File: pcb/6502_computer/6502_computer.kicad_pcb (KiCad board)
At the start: 2 copper layers, 116.8 x 73.7 mm, 44 parts, among them J1 Conn_02x04_Odd_Even, J2 USB_B, J3 Conn_02x20_Odd_Even, J4 Conn_01x04, J5 Conn_01x02, SW1 SW_Push, SW2 SW_Push, SW3 SW_Push, U1 6502, U10 CH340N, U11 MC6840, U2 6551, U3 74LS139, U4 74LS138, U5 CY62256-70PC, U6 27C64, U7 74LS00, U8 DS1813-5+, U9 74LS93, X1 ACO-xxxMHz, Y1 1.8432MHz

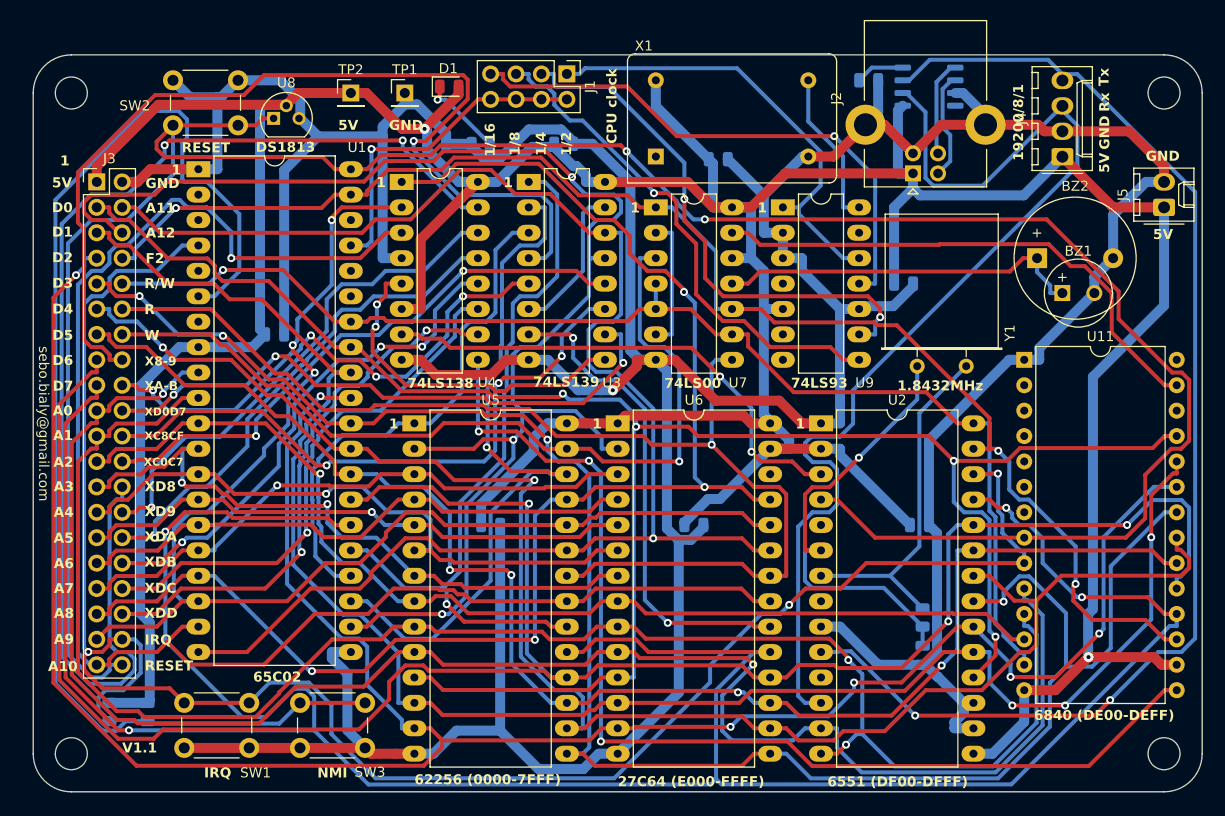
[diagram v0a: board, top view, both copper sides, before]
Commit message: silkscreen fixes
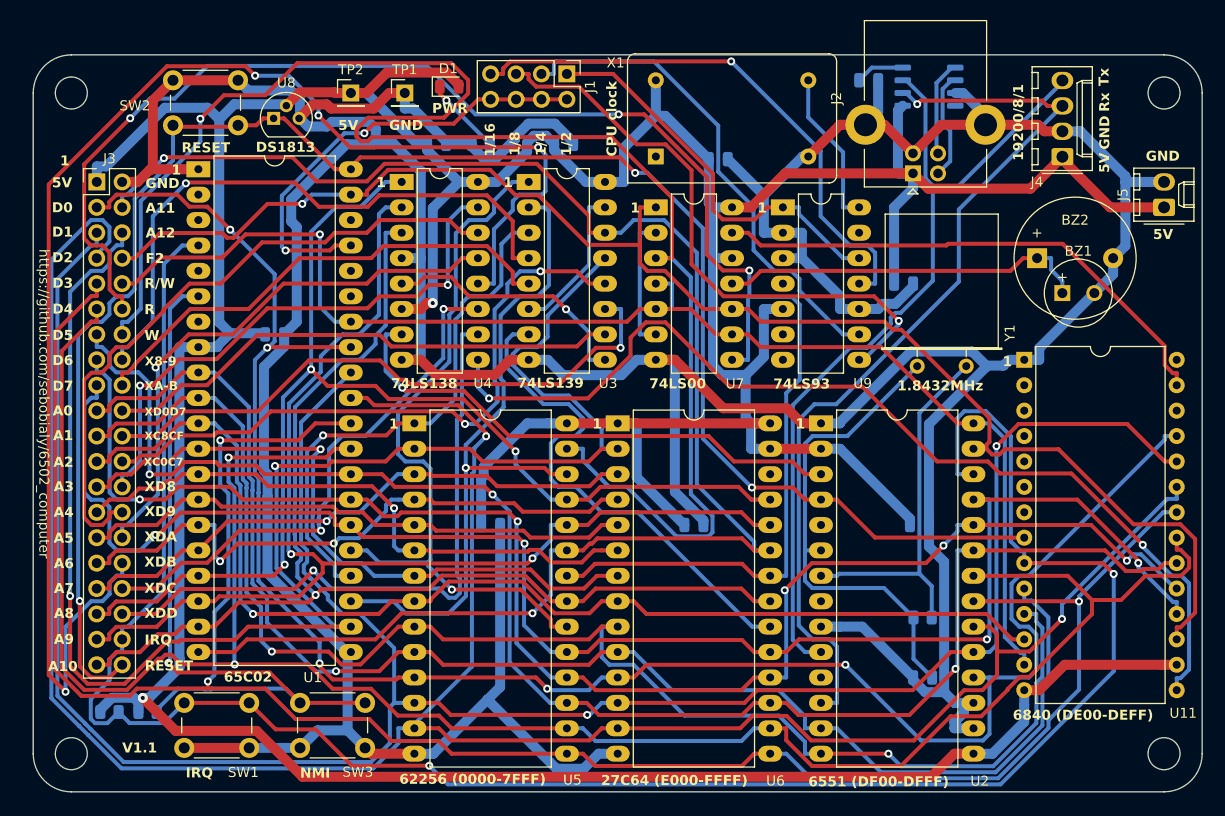
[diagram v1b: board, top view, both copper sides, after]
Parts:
- moved C1 2.22 mm to (153.7, 99.1), turned to 0 degrees
- turned R1 to 180 degrees
- turned R2 to 180 degrees
- turned R4 to 180 degrees
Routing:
- net /D7: track 272.1 -> 162.2 mm
- net /XDB: track 51.2 -> 144.4 mm, vias 3 -> 4
- net /W: track 86.5 -> 161.4 mm
- net /RES: track 247.4 -> 181.0 mm, vias 2 -> 3
- net /XD8: track 122.1 -> 56.1 mm
- net /D6: track 215.7 -> 153.3 mm, vias 3 -> 5
- net /D1: track 176.2 -> 233.5 mm, vias 3 -> 2
- net VCC: track 435.5 -> 488.0 mm
- net /D4: track 166.4 -> 218.2 mm
- net /R: track 115.8 -> 167.1 mm, vias 1 -> 3
- net /NMI: track 124.0 -> 76.2 mm, vias 0 -> 1
- net /A10: track 158.7 -> 117.2 mm
- net /TxD: track 124.1 -> 85.2 mm, vias 2 -> 0
- net /D3: track 187.9 -> 226.1 mm, vias 4 -> 3
- net /X89: track 98.3 -> 61.1 mm
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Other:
- board text added: "PWR"
- board text added: "https://github.com/sebobialy/6502_computer"
- board text removed: "sebo.bialy@gmail.com"

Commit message: added timer outputs from 6840
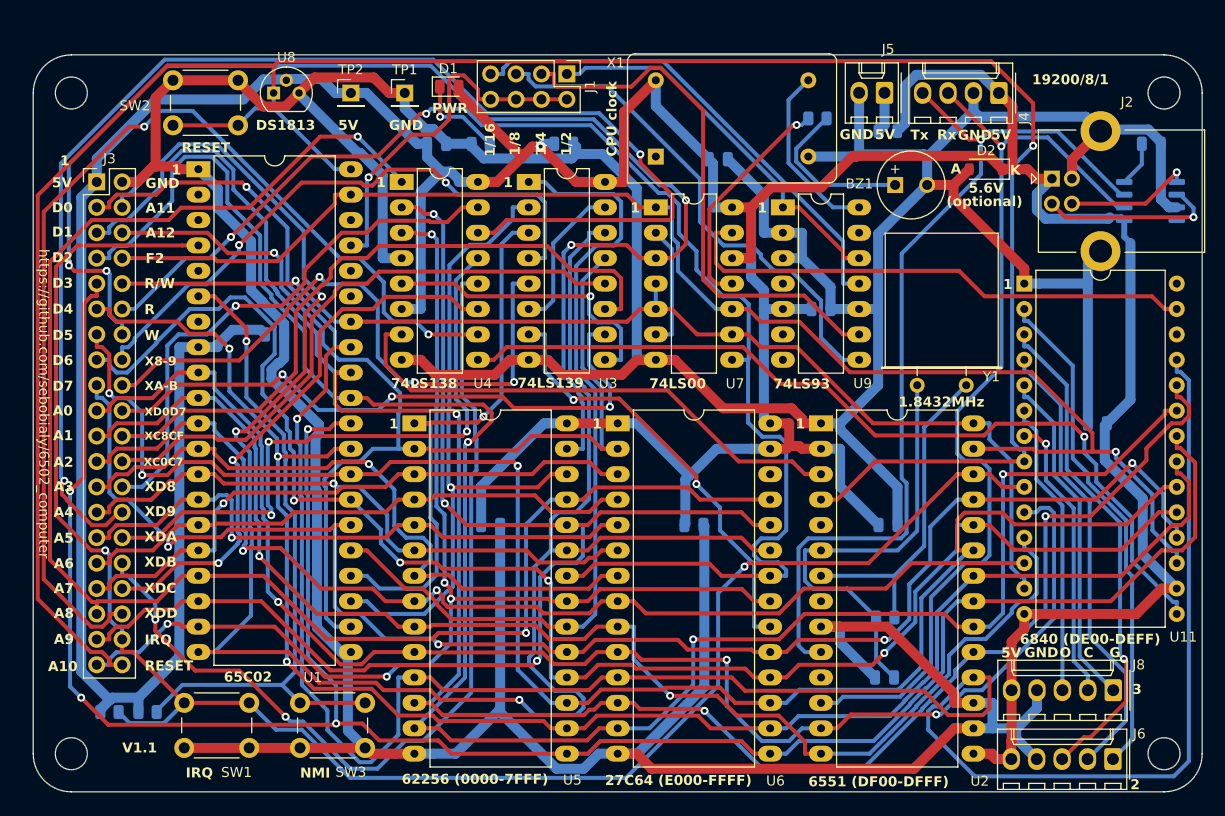
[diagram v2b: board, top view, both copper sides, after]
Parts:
- removed BZ2: Buzzer, Buzzer_Beeper:Buzzer_12x9.5RM7.6
- added C11: 100n, Capacitor_SMD:C_0805_2012Metric, B.Cu at (171.1, 73.7)
- added D2: 5.6V, Diode_SMD:D_SOD-123, F.Cu at (160.0, 48.3)
- added F1: Polyfuse, Fuse:Fuse_0805_2012Metric, B.Cu at (150.2, 44.5)
- added J6: Conn_01x05, Connector_Molex:Molex_KK-254_AE-6410-05A_1x05_P2.54mm_Vertical, F.Cu at (172.7, 107.2)
- added J8: Conn_01x05, Connector_Molex:Molex_KK-254_AE-6410-05A_1x05_P2.54mm_Vertical, F.Cu at (172.7, 100.3)
- added R5: 1k, Resistor_SMD:R_0805_2012Metric, B.Cu at (143.2, 43.2)
- moved J5 30.2 mm to (149.9, 40.6), turned to 180 degrees
- moved C2 29.0 mm to (176.5, 45.7)
- moved U10 24.9 mm to (176.4, 51.4)
- moved BZ1 19.9 mm to (150.9, 49.8)
- moved J2 13.9 mm to (166.6, 49.2), turned to 0 degrees
- moved J4 8.99 mm to (161.3, 40.6), turned to 180 degrees
- moved C10 8.64 mm to (143.5, 62.2)
- moved U11 7.62 mm to (163.8, 59.7)
- moved C1 3.81 mm to (149.9, 99.1)
- moved R4 3.74 mm to (149.9, 93.1)
- moved C5 3.14 mm to (150.2, 83.8)
- moved U8 2.54 mm to (88.8, 40.6)
- moved Y1 1.91 mm to (158.0, 69.8)
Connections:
- J5 pad 1: VCC -> /5V
- U11 pad 2: unconnected-(U11-~{G2}-Pad2) -> Net-(J6-Pin_1)
- U11 pad 3: unconnected-(U11-O2-Pad3) -> Net-(J6-Pin_3)
- U11 pad 4: unconnected-(U11-~{C2}-Pad4) -> Net-(J6-Pin_2)
- U11 pad 5: unconnected-(U11-~{G3}-Pad5) -> Net-(J8-Pin_1)
- U11 pad 6: unconnected-(U11-O3-Pad6) -> Net-(J8-Pin_3)
- U11 pad 7: unconnected-(U11-~{C3}-Pad7) -> Net-(J8-Pin_2)
- U7 pad 11: Net-(BZ1-+) -> Net-(R5-Pad1)
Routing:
- net GND: track 507.5 -> 581.2 mm
- net /XD9: track 66.0 -> 135.1 mm, vias 0 -> 2
- net /RES: track 181.0 -> 243.2 mm, vias 3 -> 1
- net /XDB: track 144.4 -> 92.2 mm, vias 4 -> 2
- net /A12: track 164.5 -> 113.5 mm, vias 2 -> 1
- net Net-(J6-Pin_1): track 0.00 -> 50.5 mm
- net Net-(J6-Pin_3): track 0.00 -> 49.9 mm, vias 0 -> 1
- net /D4: track 218.2 -> 168.9 mm, vias 2 -> 3
- net /D0: track 190.9 -> 239.6 mm, vias 5 -> 2
- net Net-(J6-Pin_2): track 0.00 -> 45.9 mm
- net /A8: track 119.9 -> 163.8 mm, vias 3 -> 2
- net /XDD: track 64.7 -> 105.9 mm, vias 1 -> 2
- net /D2: track 241.1 -> 200.7 mm, vias 2 -> 3
- net Net-(J8-Pin_1): track 0.00 -> 34.4 mm
- net /D1: track 233.5 -> 200.1 mm, vias 2 -> 3
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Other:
- board text added: "(optional)"
- board text added: "2"
- board text added: "3"
- board text added: "5.6V"
- board text added: "A"
- board text added: "C"
- board text added: "G"
- board text added: "K"
- board text added: "O"

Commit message: fixed problem with not negating E for 74LS139. Buzzer is now using a transistor. 6502 is ZIF friendly.
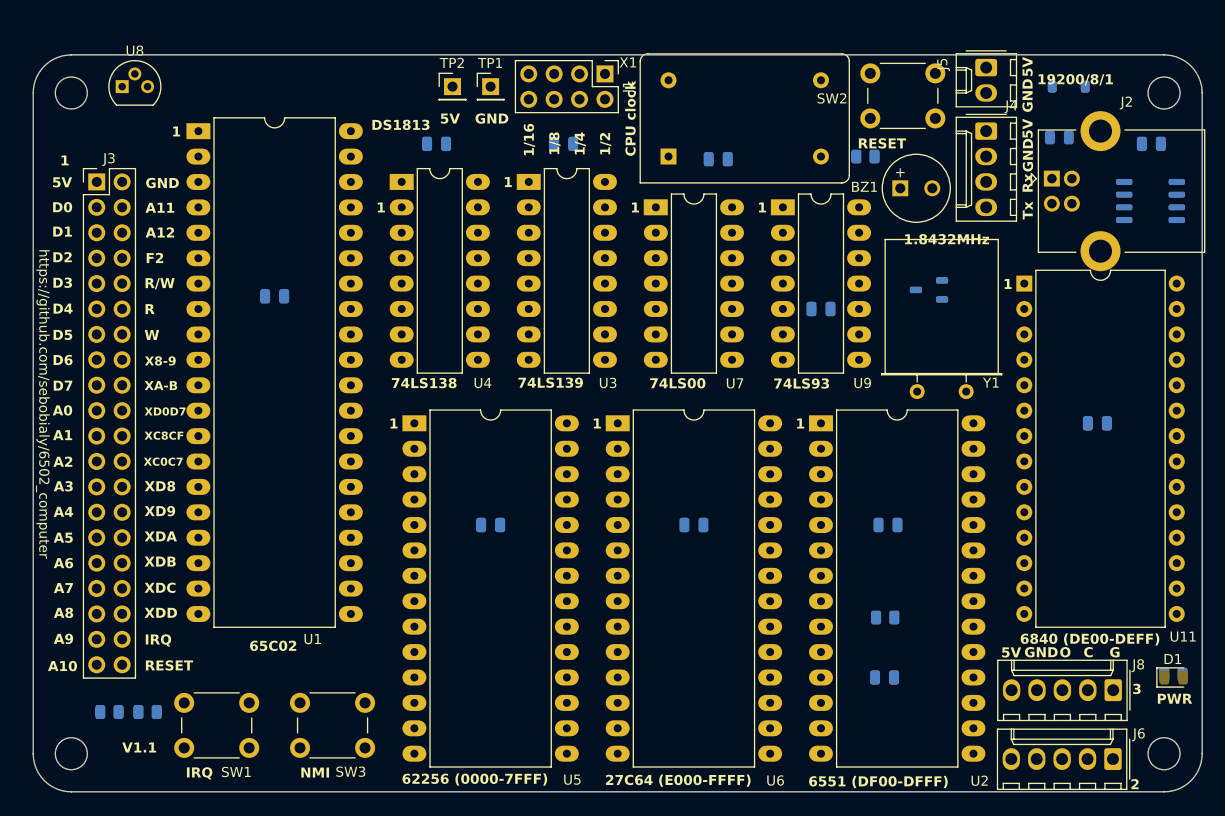
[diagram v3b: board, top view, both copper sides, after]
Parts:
- added Q1: NPN, Package_TO_SOT_SMD:TSOT-23, B.Cu at (154.3, 60.3)
- D2: moved to B.Cu
- moved D1 93.4 mm to (178.8, 99.1)
- moved R3 87.2 mm to (178.7, 98.8)
- moved SW2 69.7 mm to (148.4, 38.7)
- moved F1 17.2 mm to (167.3, 45.1)
- moved U8 15.2 mm to (73.7, 40.0)
- moved D2 11.7 mm to (168.3, 40.0), turned to 0 degrees
- moved J5 10.5 mm to (160.0, 38.1), turned to -90 degrees
- moved TP2 10.2 mm to (106.7, 40.0)
- moved TP1 8.61 mm to (110.5, 40.0)
- moved R5 6.13 mm to (148.0, 47.0)
- moved J4 4.02 mm to (160.0, 44.5), turned to -90 degrees
- moved J1 3.81 mm to (121.9, 38.7)
- moved U1 3.80 mm to (81.3, 44.5)
- moved C7 3.80 mm to (88.9, 61.0)
- moved X1 1.27 mm to (128.3, 47.0)
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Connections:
- BZ1 pad 1: Net-(BZ1-+) -> VCC
- BZ1 pad 2: GND -> Net-(BZ1--)
- R5 pad 1: Net-(R5-Pad1) -> /BUZZ
- R5 pad 2: Net-(BZ1-+) -> Net-(Q1-B)
- U3 pad 1: /A15 -> Net-(U3A-E)
- U7 pad 11: Net-(R5-Pad1) -> Net-(U3A-E)
- U7 pad 12: VCC -> /A15
- U7 pad 13: /BUZZ -> /A15
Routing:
- net GND: track 581.2 -> 0.00 mm
- net VCC: track 472.1 -> 0.00 mm, vias 1 -> 0
- net /RES: track 243.2 -> 0.00 mm, vias 1 -> 0
- net /D0: track 239.6 -> 0.00 mm, vias 2 -> 0
- net /D3: track 216.7 -> 0.00 mm, vias 4 -> 0
- net /D2: track 200.7 -> 0.00 mm, vias 3 -> 0
- net /D1: track 200.1 -> 0.00 mm, vias 3 -> 0
- net /A11: track 197.8 -> 0.00 mm, vias 3 -> 0
- net /IRQ: track 179.2 -> 0.00 mm, vias 2 -> 0
- net /D4: track 168.9 -> 0.00 mm, vias 3 -> 0
- net /D5: track 164.1 -> 0.00 mm, vias 3 -> 0
- net /A8: track 163.8 -> 0.00 mm, vias 2 -> 0
- net /D6: track 157.3 -> 0.00 mm, vias 4 -> 0
- net /D7: track 153.1 -> 0.00 mm, vias 4 -> 0
- net /A0: track 146.2 -> 0.00 mm, vias 3 -> 0
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
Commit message: routed 1.2 version
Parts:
- moved U8 34.8 mm to (108.0, 45.7)
- moved C6 2.86 mm to (102.2, 45.7)
- moved J3 1.27 mm to (69.8, 49.5)
- moved H2 1.27 mm to (67.3, 106.7)
- moved H4 1.27 mm to (67.3, 40.6)
- moved SW1 0.93 mm to (86.4, 107.0)
- moved SW3 0.93 mm to (97.9, 107.0)
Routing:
- net GND: track 0.00 -> 562.6 mm, vias 0 -> 1
- net VCC: track 0.00 -> 484.4 mm, vias 0 -> 4
- net /D1: track 0.00 -> 268.0 mm, vias 0 -> 3
- net /D2: track 0.00 -> 229.0 mm, vias 0 -> 3
- net /D3: track 0.00 -> 215.6 mm
- net /D4: track 0.00 -> 207.3 mm, vias 0 -> 3
- net /D0: track 0.00 -> 204.8 mm, vias 0 -> 2
- net /D6: track 0.00 -> 202.6 mm, vias 0 -> 3
- net /D7: track 0.00 -> 195.3 mm, vias 0 -> 4
- net /RES: track 0.00 -> 192.4 mm, vias 0 -> 1
- net /D5: track 0.00 -> 180.6 mm, vias 0 -> 4
- net /IRQ: track 0.00 -> 176.6 mm, vias 0 -> 2
- net /R: track 0.00 -> 163.5 mm, vias 0 -> 3
- net /W: track 0.00 -> 150.6 mm, vias 0 -> 4
- net /A11: track 0.00 -> 148.3 mm
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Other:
- board size 116.8 x 73.7 mm -> 118.1 x 73.7 mm
- board text added: "V1.2"
- board text removed: "V1.1"

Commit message: routed v1.2
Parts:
- moved U4 1.27 mm to (102.9, 49.5)
- moved C10 0.65 mm to (142.9, 62.2)
- moved U9 0.65 mm to (139.1, 52.1)
- moved U3 0.62 mm to (114.9, 49.5)
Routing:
- net /XD0D7: track 130.5 -> 54.2 mm, vias 3 -> 1
- net /W: track 150.6 -> 86.4 mm, vias 4 -> 3
- net /D6: track 202.6 -> 145.2 mm, vias 3 -> 2
- net /D7: track 195.3 -> 141.1 mm, vias 4 -> 2
- net /R: track 163.5 -> 110.6 mm, vias 3 -> 0
- net /XC8CF: track 61.1 -> 111.1 mm
- net /D3: track 215.6 -> 170.3 mm, vias 0 -> 2
- net /D4: track 207.3 -> 165.2 mm, vias 3 -> 2
- net GND: track 562.6 -> 527.4 mm, vias 1 -> 2
- net /A11: track 148.3 -> 183.4 mm, vias 0 -> 1
- net VCC: track 484.4 -> 452.6 mm, vias 4 -> 2
- net /D1: track 268.0 -> 237.9 mm, vias 3 -> 4
- net /D5: track 180.6 -> 151.1 mm, vias 4 -> 2
- net /XDC: track 85.0 -> 61.6 mm, vias 2 -> 3
- net /XDD: track 54.6 -> 74.6 mm, vias 3 -> 1
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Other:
- board text added: "B"
- board text added: "E"
- board text added: "NPN"

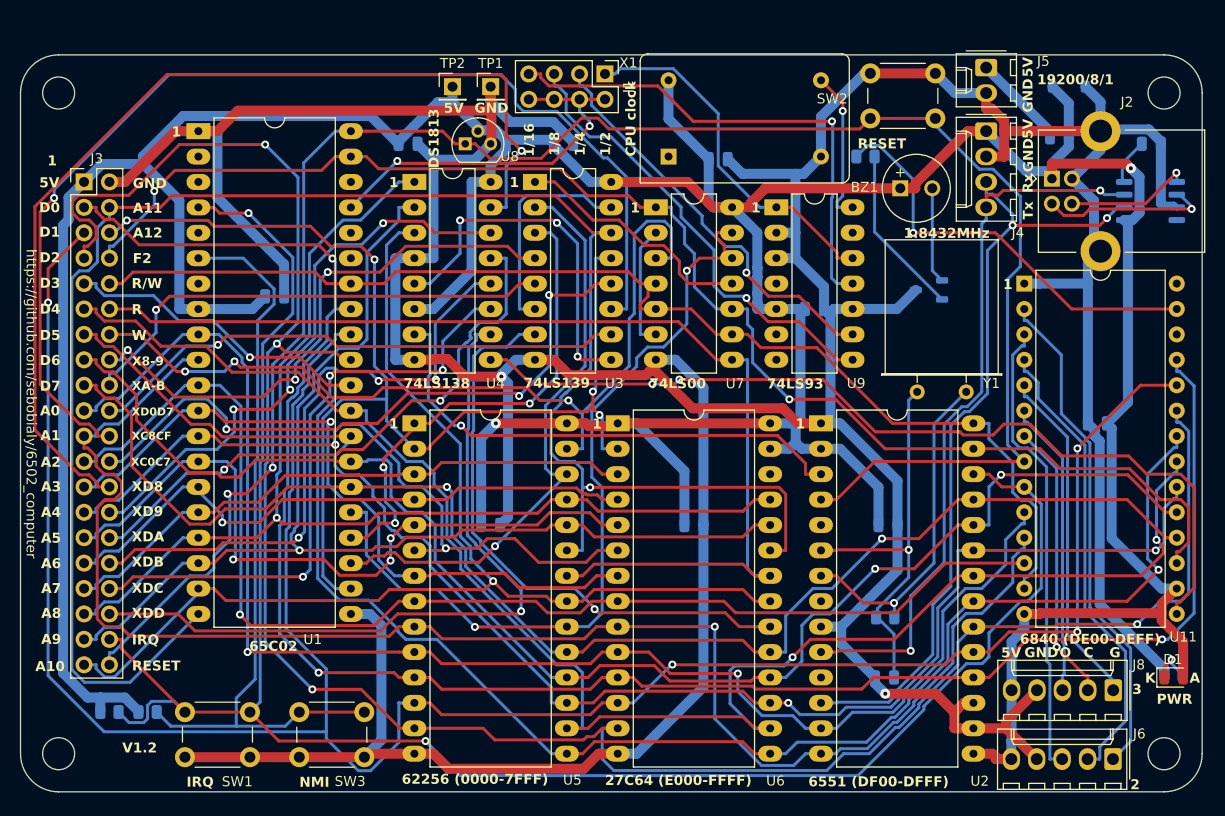
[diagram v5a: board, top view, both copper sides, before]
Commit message: v1.2 label fixes, pullup resistors for uart, routed
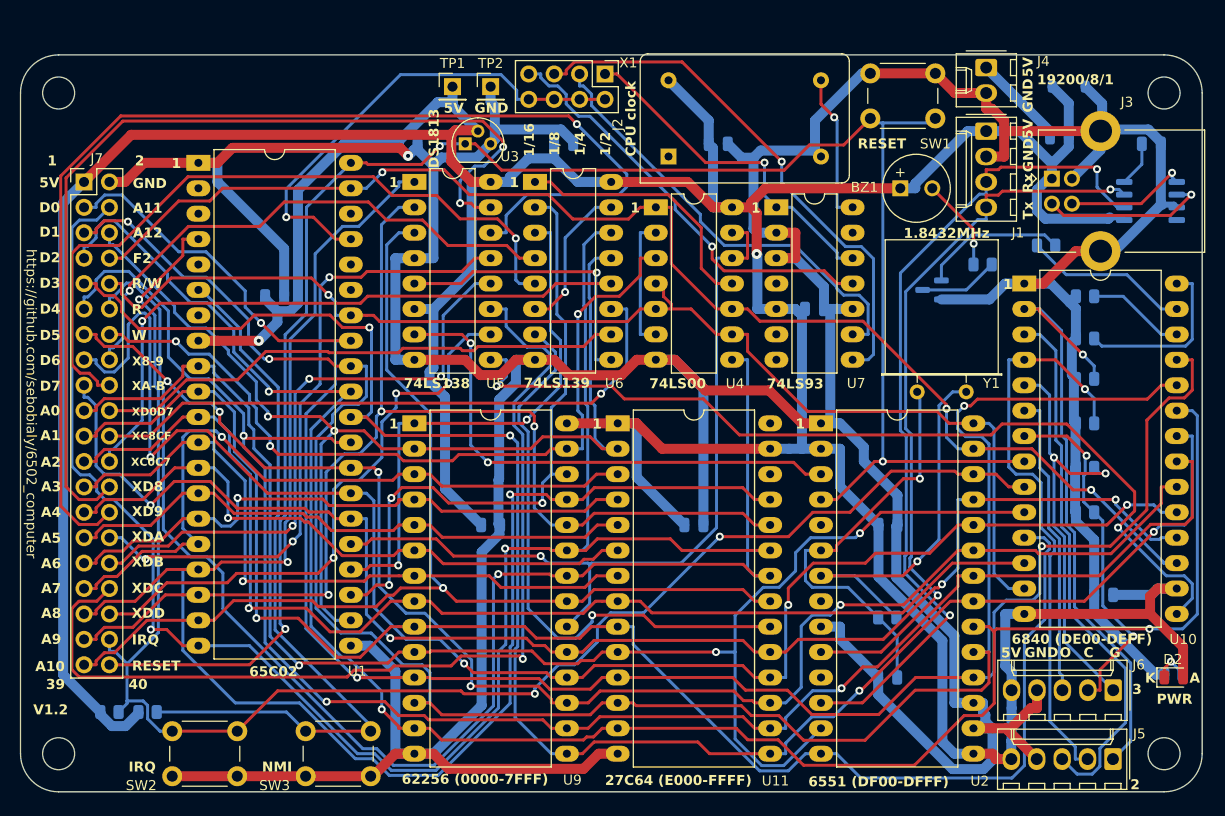
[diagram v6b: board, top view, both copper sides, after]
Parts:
- added R10: 10k, Resistor_SMD:R_0805_2012Metric, B.Cu at (169.9, 82.5)
- added R11: 10k, Resistor_SMD:R_0805_2012Metric, B.Cu at (169.9, 61.0)
- added R12: 10k, Resistor_SMD:R_0805_2012Metric, B.Cu at (169.9, 65.2)
- added R5: 220, Resistor_SMD:R_0805_2012Metric, B.Cu at (159.7, 57.8)
- added R7: 10k, Resistor_SMD:R_0805_2012Metric, B.Cu at (169.9, 69.2)
- added R8: 10k, Resistor_SMD:R_0805_2012Metric, B.Cu at (169.9, 73.7)
- added R9: 10k, Resistor_SMD:R_0805_2012Metric, B.Cu at (169.9, 78.1)
- Q1: value NPN -> BC817; footprint Package_TO_SOT_SMD:TSOT-23 -> Package_TO_SOT_SMD:SOT-23
- U10: renamed from U11; footprint Package_DIP:DIP-28_W15.24mm -> Package_DIP:DIP-28_W15.24mm_LongPads
- moved R4 20.1 mm to (166.0, 55.9)
- moved C10 17.2 mm to (171.8, 90.8)
- moved U1 3.17 mm to (81.3, 47.6)
- moved SW2 2.29 mm to (85.2, 108.9)
- moved SW3 2.01 mm to (98.5, 108.9)
- moved C8 1.54 mm to (133.2, 45.7)
- moved C1 0.31 mm to (150.2, 99.1)
- moved Q1 0.30 mm to (154.6, 60.3)
- moved R1 0.21 mm to (150.1, 93.1)
- renumbered C11 to C10, C2 to C11, C3 to C2, C4 to C3, C5 to C4, C6 to C5, C7 to C6, C8 to C7, C9 to C8, C10 to C9, D2 to D1, D1 to D2, H4 to H1, H1 to H2, H2 to H3, H3 to H4, J4 to J1, J1 to J2, J2 to J3, J5 to J4, J6 to J5, J8 to J6, J3 to J7, R4 to R1, R1 to R2, R2 to R3, R5 to R4, R3 to R6, SW2 to SW1, SW1 to SW2, TP2 to TP1, TP1 to TP2, U6 to U11, U8 to U3, U7 to U4, U4 to U5, U3 to U6, U9 to U7, U10 to U8, U5 to U9
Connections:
- Q1 pad 1: Net-(BZ1--) -> Net-(Q1-B)
- Q1 pad 2: Net-(Q1-B) -> GND
- Q1 pad 3: GND -> Net-(Q1-C)
- U10 pad 26: unconnected-(U11-~{G1}-Pad26) -> Net-(U10-~{G1})
- U10 pad 28: unconnected-(U11-~{C1}-Pad28) -> Net-(U10-~{C1})
- U11 pad 28: VCC -> unconnected-(U11-VCC-Pad28)
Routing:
- net /XD9: track 58.1 -> 118.4 mm, vias 3 -> 1
- net /A8: track 116.2 -> 166.8 mm, vias 1 -> 2
- net /XC8CF: track 111.1 -> 62.0 mm
- net /D1: track 237.9 -> 199.9 mm, vias 4 -> 3
- net /XDC: track 61.6 -> 98.3 mm, vias 3 -> 1
- net /R: track 110.6 -> 144.0 mm, vias 0 -> 1
- net /IRQ: track 193.0 -> 161.2 mm, vias 2 -> 3
- net /D2: track 221.5 -> 195.0 mm, vias 4 -> 3
- net /BUZZ: track 42.4 -> 16.6 mm, vias 1 -> 0
- net /XAB: track 48.8 -> 72.4 mm
- net GND: track 527.4 -> 548.7 mm, vias 2 -> 1
- net Net-(U10-~{C1}): track 0.00 -> 17.5 mm
- net VCC: track 452.6 -> 469.2 mm
- net /XDD: track 74.6 -> 58.3 mm, vias 1 -> 3
- net /D6: track 145.2 -> 159.6 mm, vias 2 -> 4
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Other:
- board text added: "10k"
- board text added: "220"
- board text added: "39"
- board text added: "40"
- board text added: "BC817"
- board text added: "RAM 0000-7FFF X8-9 8000-9FFF XA-B A000-BFFF XC0C7 C000-C7FF XC8CF C800-CFFF XD0D7 D000-D7FF XD8 D800-D8FF XD9 D900-D9FF XDA DA00-DAFF XDB DB00-DBFF XDC DC00-DCFF XDD DD00-DDFF (active low)"
- board text added: "Volume"
- board text removed: "NPN"
- board text removed: "X8-9 8000-9FFF XA-B A000-BFFF XC0C7 C000-C7FF XC8CF C800-CFFF XD0D7 D000-D7FF XD8 D800-D8FF XD9 D900-D9FF XDA DA00-DAFF XDB DB00-DBFF XDC DC00-DCFF XDD DD00-DDFF XDE DE00-DEFF"
